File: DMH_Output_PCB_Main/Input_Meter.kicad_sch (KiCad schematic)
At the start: 29 parts, among them U20 TL072, U24 LM339, U25 LM339

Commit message: Prepped for Main PCB design
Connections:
- net Meter_Left renamed L_Ext_Meter_M
- net Meter_Right renamed R_Ext_Meter_M
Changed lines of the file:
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@@
 		)
 	)
-	(hierarchical_label "Meter_Left"
+	(hierarchical_label "L_Ext_Meter_M"
 		(shape input)
 		(at 25.4 48.26 180)
@@
 		)
 	)
-	(hierarchical_label "Meter_Right"
+	(hierarchical_label "R_Ext_Meter_M"
 		(shape input)
 		(at 139.7 48.26 180)

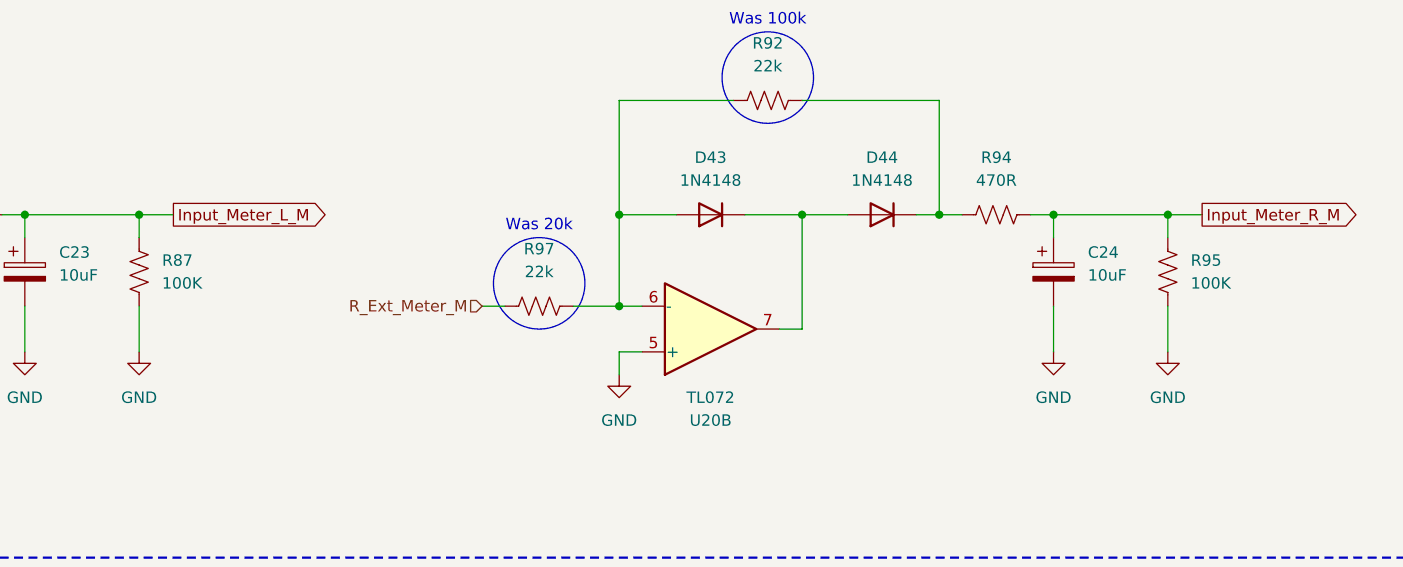
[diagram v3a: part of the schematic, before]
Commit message: PCB Main comp placement done
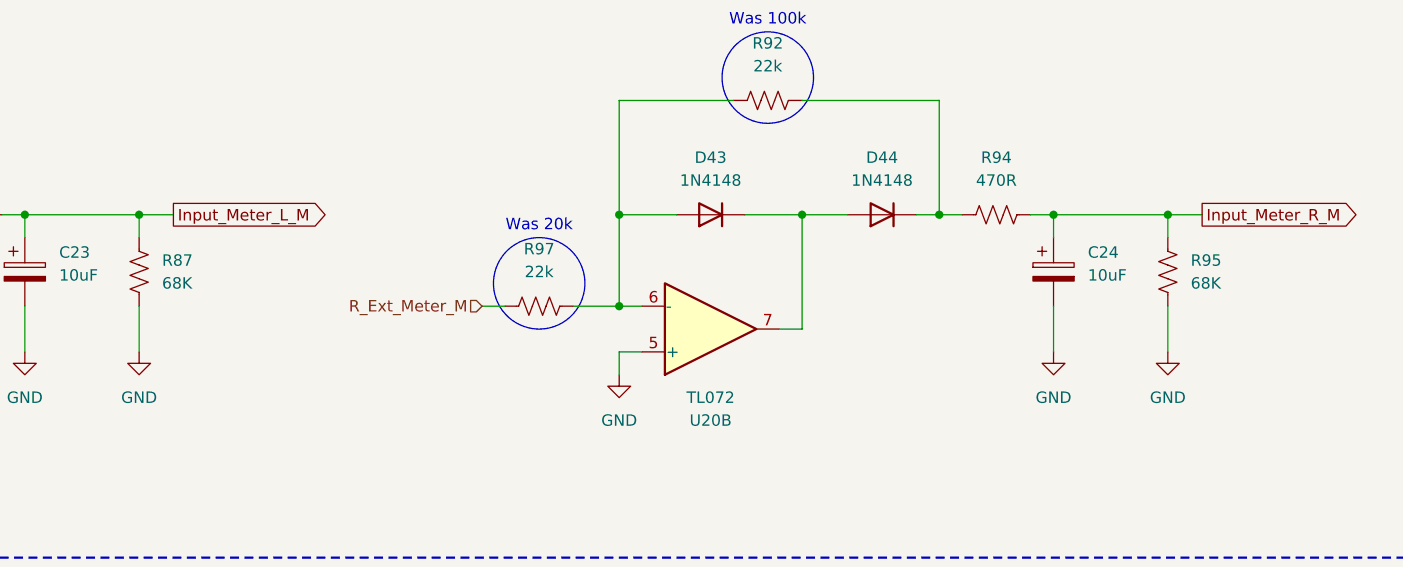
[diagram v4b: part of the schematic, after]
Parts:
- R87, R95: value 100K -> 68K
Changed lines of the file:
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@@
 			)
 		)
-		(property "Value" "100K"
+		(property "Value" "68K"
 			(at 218.44 45.7199 0)
 			(show_name no)
@@
 			)
 		)
-		(property "Value" "100K"
+		(property "Value" "68K"
 			(at 104.14 45.7199 0)
 			(show_name no)
